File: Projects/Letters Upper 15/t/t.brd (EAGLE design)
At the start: 16.5 x 21.6 mm, 27 parts

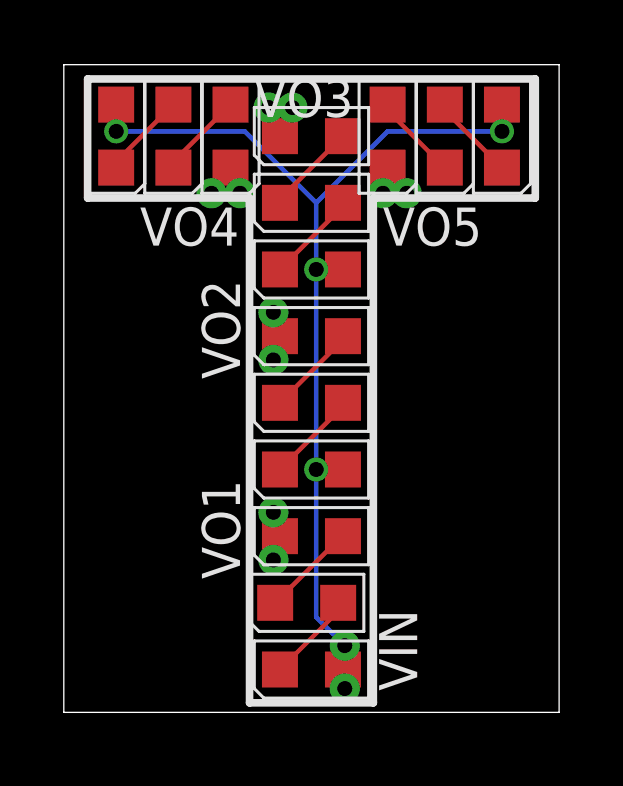
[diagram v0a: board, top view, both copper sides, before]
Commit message: 
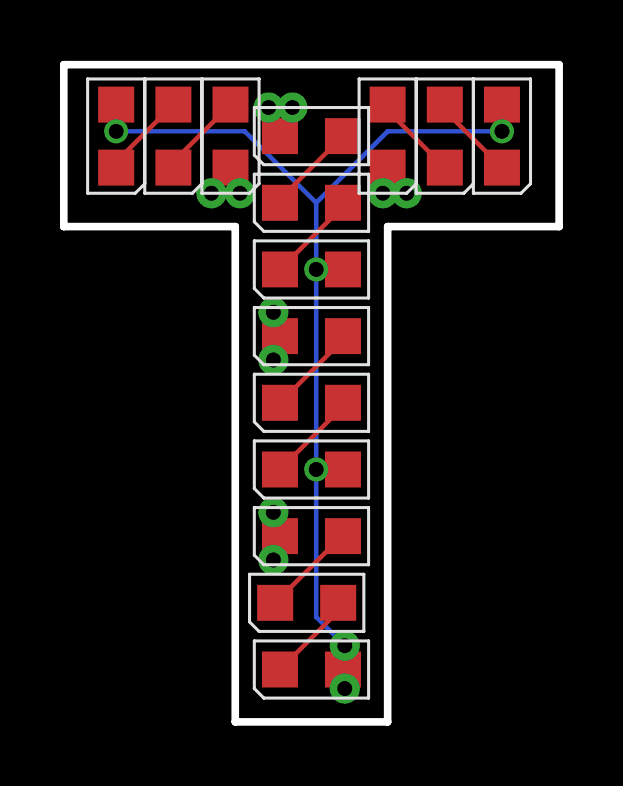
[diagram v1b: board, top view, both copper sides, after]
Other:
- board size 16.5 x 21.6 mm -> 16.5 x 21.9 mm
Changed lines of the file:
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@@
 <layer number="18" name="Vias" color="2" fill="1" visible="yes" active="yes"/>
 <layer number="19" name="Unrouted" color="6" fill="1" visible="yes" active="yes"/>
-<layer number="20" name="Dimension" color="15" fill="1" visible="yes" active="yes"/>
+<layer number="20" name="Dimension" color="3" fill="1" visible="yes" active="yes"/>
 <layer number="21" name="tPlace" color="7" fill="1" visible="yes" active="yes"/>
 <layer number="22" name="bPlace" color="7" fill="1" visible="yes" active="yes"/>
@@
 <layer number="24" name="bOrigins" color="15" fill="1" visible="yes" active="yes"/>
 <layer number="25" name="tNames" color="7" fill="1" visible="yes" active="yes"/>
-<layer number="26" name="bNames" color="7" fill="1" visible="yes" active="yes"/>
+<layer number="26" name="bNames" color="5" fill="1" visible="yes" active="yes"/>
 <layer number="27" name="tValues" color="7" fill="1" visible="yes" active="yes"/>
 <layer number="28" name="bValues" color="7" fill="1" visible="yes" active="yes"/>
@@
 <board>
 <plain>
-<wire x1="0" y1="0" x2="16.51" y2="0" width="0" layer="20"/>
-<wire x1="16.51" y1="0" x2="16.51" y2="21.59" width="0" layer="20"/>
-<wire x1="16.51" y1="21.59" x2="0" y2="21.59" width="0" layer="20"/>
-<wire x1="0" y1="21.59" x2="0" y2="0" width="0" layer="20"/>
 <text x="0.9525" y="0.3175" size="20.32" layer="201" font="fixed" ratio="15" distance="27">T</text>
-<wire x1="0.79375" y1="21.11375" x2="0.79375" y2="17.145" width="0.254" layer="21"/>
-<wire x1="0.79375" y1="17.145" x2="6.19125" y2="17.145" width="0.254" layer="21"/>
-<wire x1="6.19125" y1="17.145" x2="6.19125" y2="0.3175" width="0.254" layer="21"/>
-<wire x1="6.19125" y1="0.3175" x2="10.31875" y2="0.3175" width="0.254" layer="21"/>
-<wire x1="10.31875" y1="0.3175" x2="10.31875" y2="17.145" width="0.254" layer="21"/>
-<wire x1="10.31875" y1="17.145" x2="15.71625" y2="17.145" width="0.254" layer="21"/>
-<wire x1="15.71625" y1="17.145" x2="15.71625" y2="21.11375" width="0.254" layer="21"/>
-<wire x1="15.71625" y1="21.11375" x2="0.79375" y2="21.11375" width="0.254" layer="21"/>
+<wire x1="0" y1="21.59" x2="0" y2="16.1925" width="0.254" layer="20"/>
+<wire x1="0" y1="16.1925" x2="5.715" y2="16.1925" width="0.254" layer="20"/>
+<wire x1="5.715" y1="16.1925" x2="5.715" y2="-0.3175" width="0.254" layer="20"/>
+<wire x1="5.715" y1="-0.3175" x2="10.795" y2="-0.3175" width="0.254" layer="20"/>
+<wire x1="10.795" y1="-0.3175" x2="10.795" y2="16.1925" width="0.254" layer="20"/>
+<wire x1="10.795" y1="16.1925" x2="16.51" y2="16.1925" width="0.254" layer="20"/>
+<wire x1="16.51" y1="16.1925" x2="16.51" y2="21.59" width="0.254" layer="20"/>
+<wire x1="16.51" y1="21.59" x2="0" y2="21.59" width="0.254" layer="20"/>
 <wire x1="8.09625" y1="3.01625" x2="8.09625" y2="2.06375" width="0.0508" layer="202"/>
 </plain>
@@
 </element>
 <element name="VIN" library="CyberRailGuru" package="P1-20" value="" x="9.36625" y="0.79375" smashed="yes">
-<attribute name="NAME" x="10.50925" y="3.429" size="1.27" layer="25" ratio="15" rot="R270"/>
+<attribute name="NAME" x="7.62" y="3.175" size="1.27" layer="26" ratio="15" rot="R270"/>
 <attribute name="VALUE" x="7.84225" y="-1.23825" size="1.27" layer="27" ratio="10"/>
 </element>
 <element name="VO1" library="CyberRailGuru" package="P1-20" value="" x="6.985" y="5.08" smashed="yes">
-<attribute name="NAME" x="5.87375" y="4.445" size="1.27" layer="25" ratio="15" rot="R90"/>
+<attribute name="NAME" x="8.89" y="4.445" size="1.27" layer="26" ratio="15" rot="R90"/>
 <attribute name="VALUE" x="5.461" y="3.048" size="1.27" layer="27" ratio="10"/>
 </element>
 <element name="VO2" library="CyberRailGuru" package="P1-20" value="" x="6.985" y="11.7475" smashed="yes">
-<attribute name="NAME" x="5.87375" y="11.1125" size="1.27" layer="25" ratio="15" rot="R90"/>
+<attribute name="NAME" x="8.89" y="10.795" size="1.27" layer="26" ratio="15" rot="R90"/>
 <attribute name="VALUE" x="5.461" y="9.7155" size="1.27" layer="27" ratio="10"/>
 </element>
 <element name="VO3" library="CyberRailGuru" package="P1-20" value="" x="6.82625" y="20.16125" smashed="yes">
-<attribute name="NAME" x="6.35" y="19.84375" size="1.27" layer="25" ratio="15"/>
+<attribute name="NAME" x="8.255" y="19.685" size="1.27" layer="26" ratio="15"/>
 <attribute name="VALUE" x="5.30225" y="18.12925" size="1.27" layer="27" ratio="10"/>
 </element>
 <element name="VO4" library="CyberRailGuru" package="P1-20" value="" x="4.92125" y="17.30375" smashed="yes">
-<attribute name="NAME" x="2.54" y="15.5575" size="1.27" layer="25" ratio="15"/>
+<attribute name="NAME" x="0.9525" y="16.8275" size="1.27" layer="26" ratio="15"/>
 <attribute name="VALUE" x="3.39725" y="15.27175" size="1.27" layer="27" ratio="10"/>
 </element>
@@
 </element>
 <element name="VO5" library="CyberRailGuru" package="P1-20" value="" x="10.63625" y="17.30375" smashed="yes">
-<attribute name="NAME" x="10.63625" y="15.5575" size="1.27" layer="25" ratio="15"/>
+<attribute name="NAME" x="12.065" y="16.8275" size="1.27" layer="26" ratio="15"/>
 <attribute name="VALUE" x="9.11225" y="15.27175" size="1.27" layer="27" ratio="10"/>
 </element>
